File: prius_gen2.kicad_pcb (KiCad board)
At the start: 4 copper layers, 147.8 x 65 mm, 152 parts, among them J1 Conn_02x05_Odd_Even, J2 Conn_01x06, J3 Conn_01x23, J4 Conn_01x14, J5 Conn_01x03_Male, Q1 IRLZ14SPBF, Q2 IRLZ14SPBF, SW1 SW_Push, SW2 SW_Push, SW3 RESET, SW4 BOOT, U2 MCP602, U3 ULN2003A, U4 TDA2822D, U5 TJA1051T-3, U6 ESP32-WROOM-32, U7 LMR14020, U8 AZ1117-3.3, U9 STM32F103VBTx, Y1 8MHz

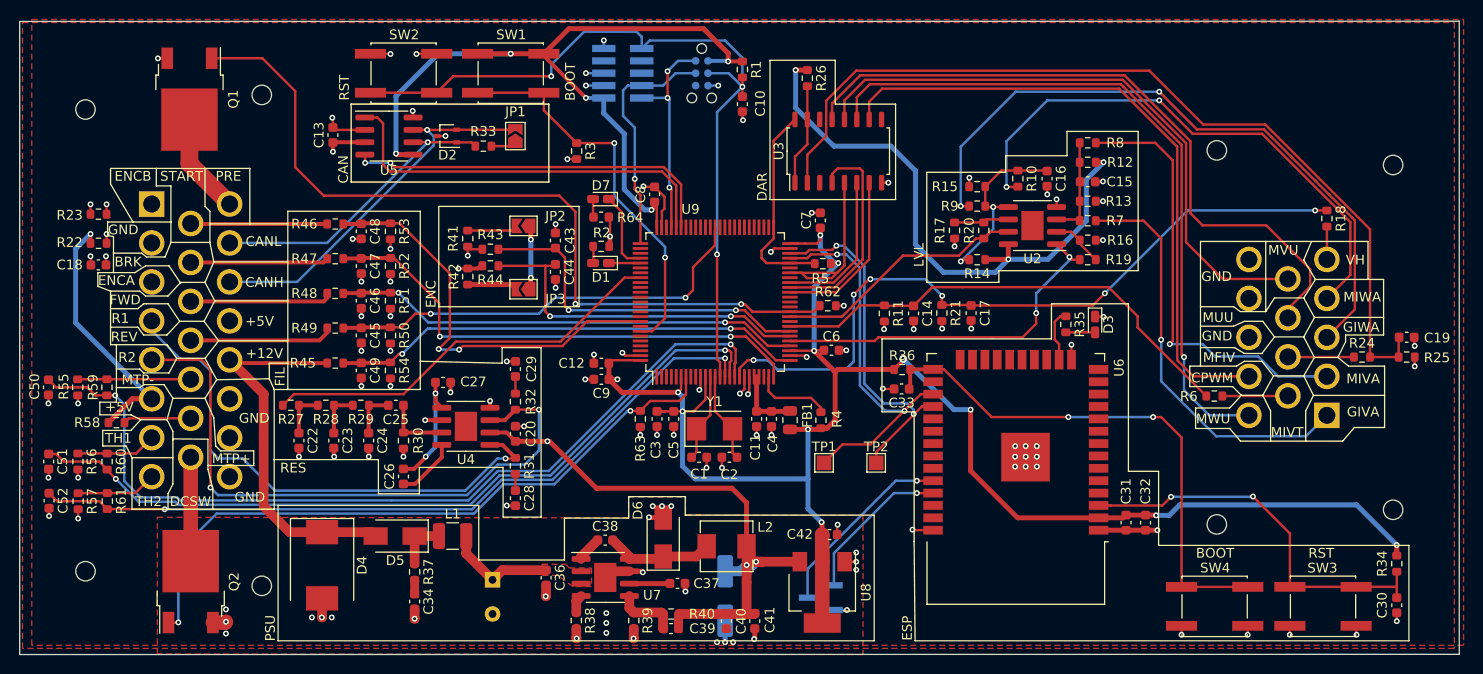
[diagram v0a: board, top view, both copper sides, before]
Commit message: fixed schematics error
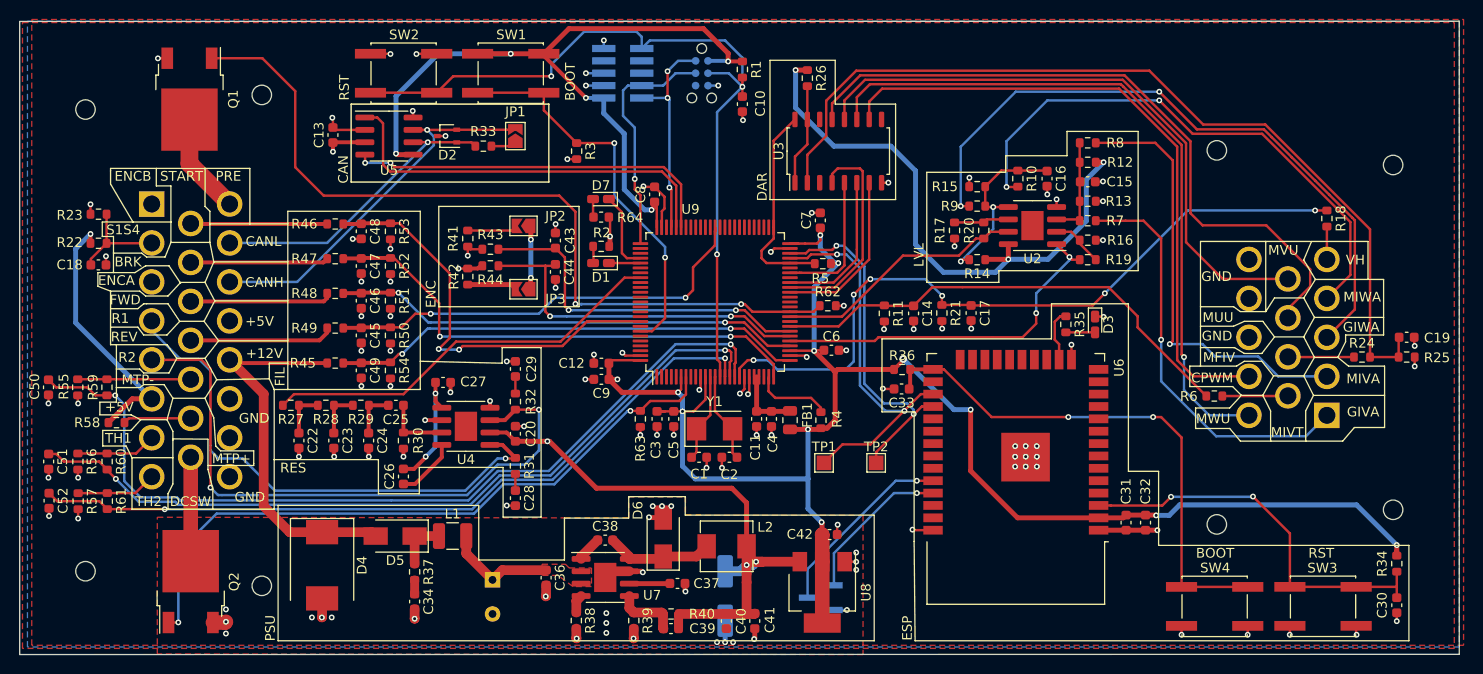
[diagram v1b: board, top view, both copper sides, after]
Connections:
- C18 pad 1: GND -> Net-(C18-Pad1)
- J3 pad 2: GND -> Net-(C18-Pad1)
- R22 pad 2: GND -> Net-(C18-Pad1)
- R23 pad 2: GND -> Net-(C18-Pad1)
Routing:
- net Net-(C18-Pad1): track 0.00 -> 10.5 mm
- net /TIM1_CH3: track 19.0 -> 14.6 mm
- net GND: track 124.6 -> 121.7 mm, vias 125 -> 122
- added copper zone on B.Cu, net GND
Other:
- board text added: "S1S4"
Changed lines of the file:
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@@
     (thickness 1.6)
     (drawings 318)
-    (tracks 1341)
+    (tracks 1336)
     (zones 0)
     (modules 152)
-    (nets 184)
+    (nets 185)
   )
   (page A4)
@@
   (net 182 "Net-(U9-Pad2)")
   (net 183 "Net-(U9-Pad1)")
+  (net 184 "Net-(C18-Pad1)")
   (net_class Default "This is the default net class."
     (clearance 0.2)
@@
     (add_net "Net-(C15-Pad1)")
     (add_net "Net-(C16-Pad1)")
+    (add_net "Net-(C18-Pad1)")
     (add_net "Net-(C19-Pad1)")
     (add_net "Net-(C2-Pad2)")
@@
       (net 74 /ENC_A))
     (pad 2 thru_hole circle (at -10 4 270) (size 2.625 2.625) (drill 1.75) (layers *.Cu *.Mask)
-      (net 2 GND))
+      (net 184 "Net-(C18-Pad1)"))
     (pad 1 thru_hole rect (at -14 4 270) (size 2.625 2.625) (drill 1.75) (layers *.Cu *.Mask)
       (net 73 /ENC_B))
@@
     )
     (pad 2 smd roundrect (at 0.825 0) (size 0.8 0.95) (layers F.Cu F.Paste F.Mask) (roundrect_rratio 0.25)
-      (net 2 GND))
+      (net 184 "Net-(C18-Pad1)"))
     (pad 1 smd roundrect (at -0.825 0) (size 0.8 0.95) (layers F.Cu F.Paste F.Mask) (roundrect_rratio 0.25)
       (net 2 GND))
@@
     )
     (pad 2 smd roundrect (at 0.825 0) (size 0.8 0.95) (layers F.Cu F.Paste F.Mask) (roundrect_rratio 0.25)
-      (net 2 GND))
+      (net 184 "Net-(C18-Pad1)"))
     (pad 1 smd roundrect (at -0.825 0) (size 0.8 0.95) (layers F.Cu F.Paste F.Mask) (roundrect_rratio 0.25)
       (net 11 +5V))
@@
       (net 2 GND))
     (pad 1 smd roundrect (at -0.775 0) (size 0.9 0.95) (layers F.Cu F.Paste F.Mask) (roundrect_rratio 0.25)
-      (net 2 GND))
+      (net 184 "Net-(C18-Pad1)"))
     (model ${KISYS3DMOD}/Capacitor_SMD.3dshapes/C_0603_1608Metric.wrl
       (at (xyz 0 0 0))
@@
       (xy -0.041674 7.552141) (xy 0.439376 7.547234)) (layer B.SilkS) (width 0.01))
   )
+  (gr_line (start 75.2475 85.0265) (end 75.2475 86.487) (layer F.SilkS) (width 0.12))
   (gr_circle (center 151.95 120.85) (end 152.1 121.05) (layer B.SilkS) (width 0.2))
   (gr_line (start 124.7 70.65) (end 124.15 70.65) (layer B.SilkS) (width 0.2))
@@
     (effects (font (size 1 1) (thickness 0.15)))
   )
-  (gr_line (start 75.8 85) (end 78.4 85) (layer F.SilkS) (width 0.12))
-  (gr_line (start 76.4 86.5) (end 76.4 88.2) (layer F.SilkS) (width 0.12))
-  (gr_line (start 75.8 86.4) (end 76.4 86.5) (layer F.SilkS) (width 0.12))
-  (gr_line (start 75.8 85) (end 75.8 86.4) (layer F.SilkS) (width 0.12))
+  (gr_line (start 75.2475 85) (end 78.4 85) (layer F.SilkS) (width 0.12))
+  (gr_line (start 76.4 86.487) (end 76.4 88.2) (layer F.SilkS) (width 0.12))
+  (gr_line (start 75.2475 86.487) (end 76.4 86.487) (layer F.SilkS) (width 0.12))
   (gr_line (start 81.7 88.6) (end 82.3 87.1) (layer F.SilkS) (width 0.12))
   (gr_line (start 79.8 88.6) (end 81.7 88.6) (layer F.SilkS) (width 0.12))
@@
     (effects (font (size 1 1) (thickness 0.15)))
   )
-  (gr_text GND (at 77.4 85.8) (layer F.SilkS)
+  (gr_text S1S4 (at 77.4 85.8) (layer F.SilkS)
     (effects (font (size 1 1) (thickness 0.15)))
   )
@@
   (segment (start 74.042 83.186) (end 74.041 83.185) (width 0.254) (layer F.Cu) (net 2))
   (segment (start 74.042 84.201) (end 74.042 83.186) (width 0.254) (layer F.Cu) (net 2))
-  (via (at 75.692 83.185) (size 0.6) (drill 0.3) (layers F.Cu B.Cu) (net 2))
-  (segment (start 75.692 84.201) (end 75.692 83.185) (width 0.254) (layer F.Cu) (net 2))
-  (via (at 75.692 86.233) (size 0.6) (drill 0.3) (layers F.Cu B.Cu) (net 2))
-  (segment (start 75.691 86.234) (end 75.692 86.233) (width 0.254) (layer F.Cu) (net 2))
-  (segment (start 75.691 87.1855) (end 75.691 86.234) (width 0.254) (layer F.Cu) (net 2))
-  (via (at 74.041 88.519) (size 0.6) (drill 0.3) (layers F.Cu B.Cu) (net 2))
-  (segment (start 74.0785 88.5565) (end 74.041 88.519) (width 0.254) (layer F.Cu) (net 2))
-  (segment (start 74.0785 89.408) (end 74.0785 88.5565) (width 0.254) (layer F.Cu) (net 2))
   (via (at 75.6285 88.519) (size 0.6) (drill 0.3) (layers F.Cu B.Cu) (net 2))
   (segment (start 75.6285 89.408) (end 75.6285 88.519) (width 0.254) (layer F.Cu) (net 2))
@@
   (segment (start 150.69959 90.218) (end 151.4475 89.47009) (width 0.25) (layer F.Cu) (net 86))
   (segment (start 151.4475 89.47009) (end 151.4475 80.974) (width 0.25) (layer F.Cu) (net 86))
-  (segment (start 150.148772 90.76599) (end 150.905631 90.009131) (width 0.254) (layer F.Cu) (net 86) (status 1000000))
-  (segment (start 147.0505 90.218) (end 147.59849 90.76599) (width 0.254) (layer F.Cu) (net 86) (status 1000000))
-  (segment (start 146.8275 90.218) (end 147.0505 90.218) (width 0.254) (layer F.Cu) (net 86) (status 1000000))
-  (segment (start 147.59849 90.76599) (end 150.148772 90.76599) (width 0.254) (layer F.Cu) (net 86))
+  (segment (start 146.8275 90.218) (end 147.0505 90.218) (width 0.254) (layer F.Cu) (net 86))
   (segment (start 152.7175 87.8205) (end 152.7175 80.974) (width 0.25) (layer F.Cu) (net 87))
   (segment (start 152.7175 88.8365) (end 152.7175 87.8205) (width 0.25) (layer F.Cu) (net 87))
@@
   (segment (start 125.6375 84.455) (end 125.6825 84.5) (width 0.254) (layer F.Cu) (net 100))
   (segment (start 125.6375 82.65) (end 125.6375 84.455) (width 0.254) (layer F.Cu) (net 100))
+  (segment (start 74.0785 88.798) (end 74.0785 89.408) (width 0.254) (layer F.Cu) (net 184))
+  (segment (start 75.691 87.1855) (end 74.0785 88.798) (width 0.254) (layer F.Cu) (net 184))
+  (segment (start 75.692 87.1845) (end 75.691 87.1855) (width 0.254) (layer F.Cu) (net 184))
+  (segment (start 75.692 84.201) (end 75.692 87.1845) (width 0.254) (layer F.Cu) (net 184))
+  (segment (start 80.2975 87.1855) (end 80.328 87.155) (width 0.254) (layer F.Cu) (net 184))
+  (segment (start 75.691 87.1855) (end 80.2975 87.1855) (width 0.254) (layer F.Cu) (net 184))
   (zone (net 2) (net_name GND) (layer F.Cu) (hatch edge 0.508)
     (priority 1)
@@
       )
     )
+  )
+  (zone (net 2) (net_name GND) (layer B.Cu) (hatch edge 0.508)
+    (connect_pads (clearance 0.508))
+    (min_thickness 0.254)
+    (fill yes (arc_segments 32) (thermal_gap 0.508) (thermal_bridge_width 0.508))
+    (polygon
+      (pts
+        (xy 214.5665 128.639) (xy 67.5665 128.639) (xy 67.5665 64.389) (xy 214.5665 64.389)
+      )
+    )

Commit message: updated routing
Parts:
- R59: value 510 -> 10k
- moved R5 6.62 mm to (146.0, 83.5)
- moved U3 1.31 mm to (152.0, 77.1), turned to 0 degrees
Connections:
- U9 pad 40: /TIM1_CH1 -> Net-(U9-Pad40)
- U9 pad 41: /TIM1_CH2N -> Net-(U9-Pad41)
- U9 pad 42: /TIM1_CH2 -> Net-(U9-Pad42)
- U9 pad 44: /TIM1_CH3 -> Net-(U9-Pad44)
- U9 pad 46: /TIM1_BKIN -> Net-(U9-Pad46)
- U9 pad 53: Net-(U9-Pad53) -> /TIM1_CH2N
- U9 pad 66: Net-(U9-Pad66) -> /TIM1_BKIN
- U9 pad 67: Net-(U9-Pad67) -> /TIM1_CH1
- U9 pad 68: Net-(U9-Pad68) -> /TIM1_CH2
- U9 pad 69: Net-(U9-Pad69) -> /TIM1_CH3
- U9 pad 78: Net-(U9-Pad78) -> Net-(D7-Pad1)
- U9 pad 79: Net-(D7-Pad1) -> Net-(U9-Pad79)
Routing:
- net /TIM1_BKIN: track 21.4 -> 30.0 mm, vias 0 -> 2
- net /TIM1_CH2N: track 22.1 -> 15.8 mm
- net Net-(J4-Pad8): track 70.4 -> 65.3 mm
- net Net-(J4-Pad9): track 62.8 -> 59.2 mm
- net /TIM1_CH3: track 14.6 -> 18.1 mm
- net +3V3: track 276.9 -> 280.1 mm
- net Net-(C19-Pad1): track 91.2 -> 88.4 mm
- net Net-(R26-Pad2): track 10.4 -> 12.6 mm
- net Net-(J4-Pad10): track 71.8 -> 69.8 mm
- net /TIM1_CH1: track 17.4 -> 15.9 mm
- net /TIM1_CH2: track 15.7 -> 17.0 mm
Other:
- board text added: "Prius G2 rev 3 2021-08"
- board text removed: "Prius G2 rev 2 2021-07"

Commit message: more routing fixes
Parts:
- moved R26 0.79 mm to (148.4, 70.0)
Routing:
- net Net-(C19-Pad1): track 88.4 -> 87.5 mm
- net +5V: track 293.3 -> 294.1 mm
- net GND: vias 122 -> 124

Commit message: updated silk and manuf. files
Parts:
- removed TP1, TP2: TestPoint, TestPoint:TestPoint_Pad_1.5x1.5mm
- moved R22 0.32 mm to (74.8, 87.5)
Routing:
- net /UART3_TX: track 39.8 -> 29.3 mm
- net /UART3_RX: track 36.4 -> 29.8 mm
- net Net-(D7-Pad1): track 8.22 -> 7.42 mm
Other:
- board text added: "COS+"
- board text added: "EXC+"
- board text added: "EXC-"
- board text added: "SIN+"
- board text added: "SIN-/COS-"
- board text removed: "ENCA"
- board text removed: "ENCB"
- board text removed: "R1"
- board text removed: "R2"
- board text removed: "S1S4"

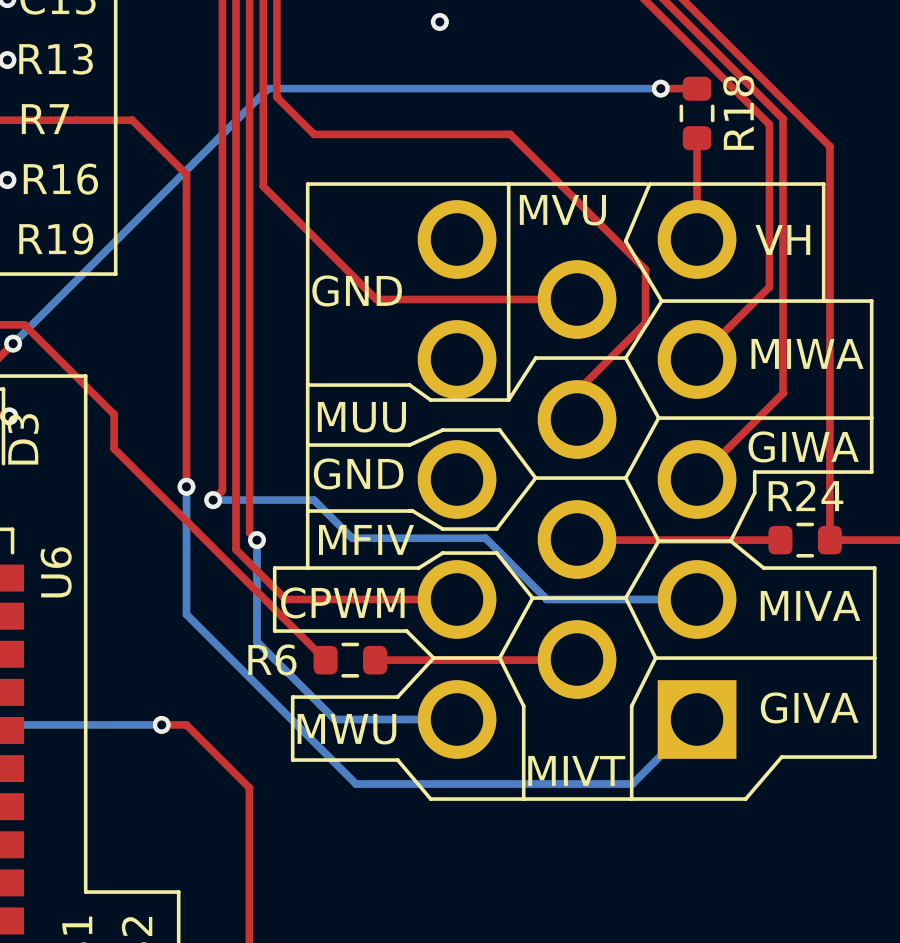
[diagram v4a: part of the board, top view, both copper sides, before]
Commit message: more updates to RC filter; fixed pinout silk
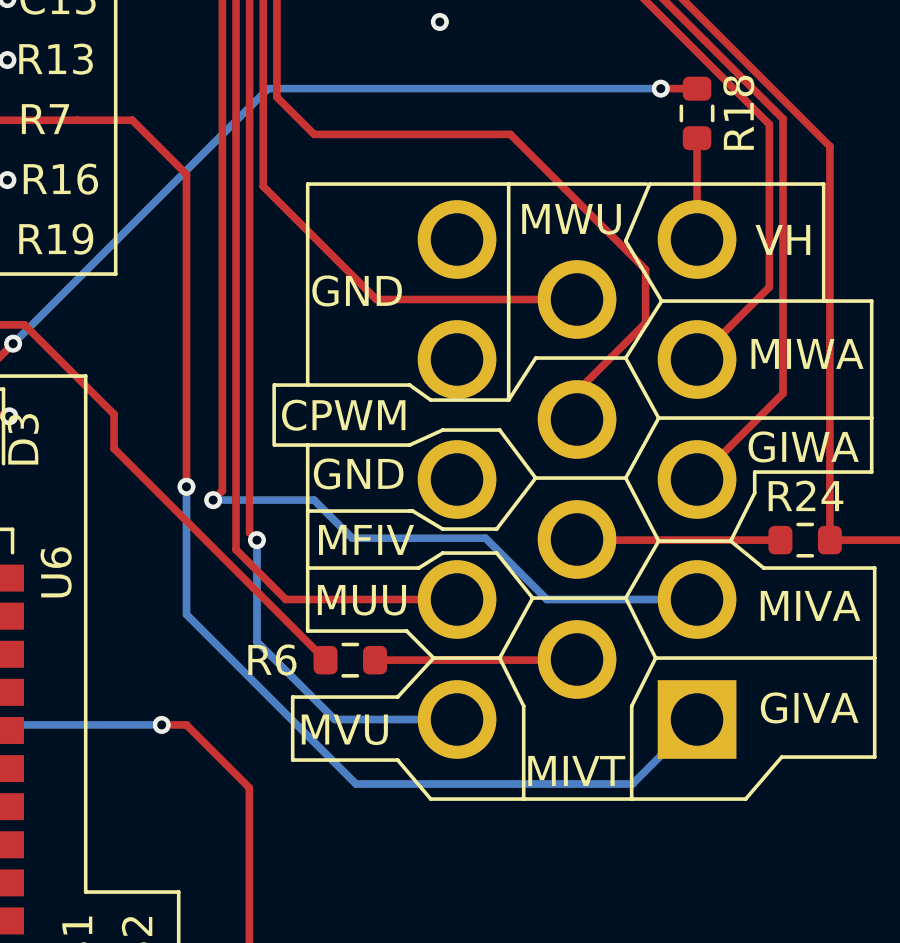
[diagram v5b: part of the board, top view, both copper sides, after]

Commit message: updates for release
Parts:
- removed G***: LOGO, rsspeed:LOGO

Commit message: updates for release
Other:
- board text added: "powered by openinverter.org github.com/ksmola/PriusG2"
- board text removed: "powered by openinverter.org"

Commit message: updates for KiCAD 6
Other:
- net class Default removed
